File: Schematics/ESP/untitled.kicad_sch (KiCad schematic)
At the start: 10 parts, among them J11 Bumper 1, J12 Bumper 2, J14 Conn_02x19_Odd_Even, J15 UltraSconic B, J16 Conn_02x19_Odd_Even, J2 IMU, J7 UltraSonic A, J8 BLE

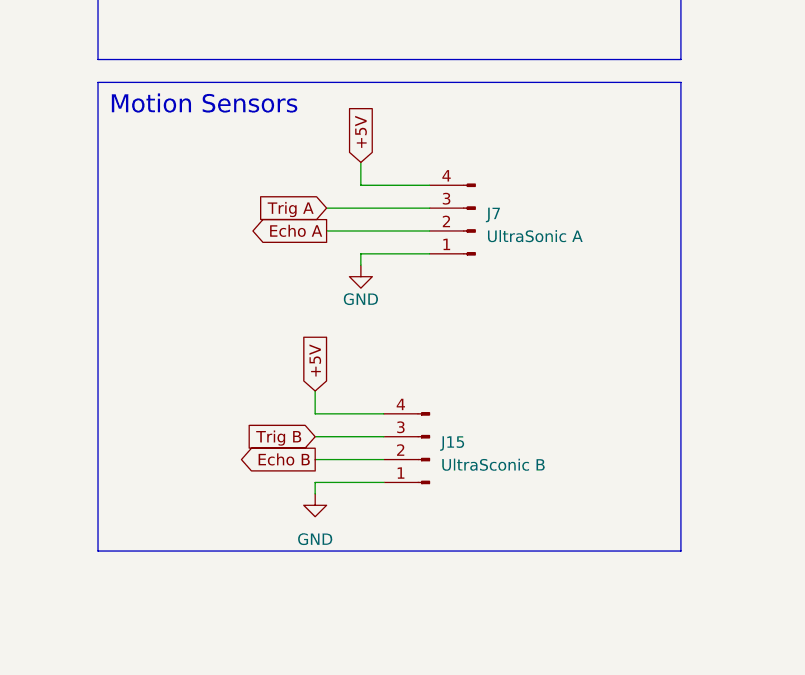
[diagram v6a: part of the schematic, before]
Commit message: PCB layout done no wiring
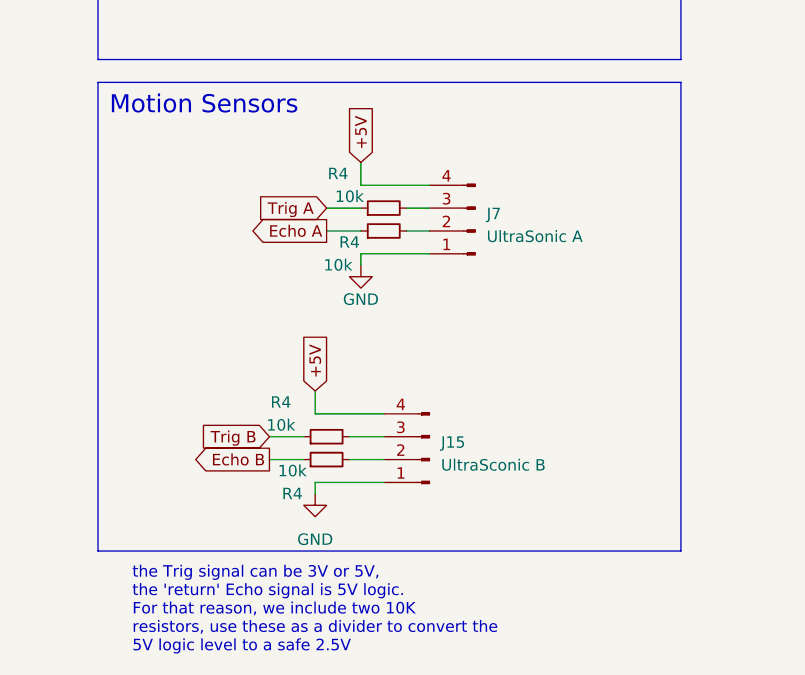
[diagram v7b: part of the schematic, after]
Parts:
- added R4 (x4): 10k, Resistor_SMD:R_1206_3216Metric_Pad1.30x1.75mm_HandSolder, symbol Device:R_Small
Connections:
- net Echo A: now also R4.1; no longer J7.2 (Pin_2)
- net Echo B: now also R4.1; no longer J15.2 (Pin_2)
- net Trig A: now also R4.1; no longer J7.3 (Pin_3)
- net Trig B: now also R4.1; no longer J15.3 (Pin_3)
- new net: J15.3 (Pin_3), R4.2
- new net: J7.3 (Pin_3), R4.2
- new net: J7.2 (Pin_2), R4.2
- new net: J15.2 (Pin_2), R4.2
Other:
- note added: "the Trig signal can be 3V or 5V, the 'return' Echo signal is 5V logic. For that reason, we include two 10K resistors, use these as a divider to convert the 5V logic level to a safe 2.5V"
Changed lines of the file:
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@@
     (stroke (width 0) (type default))
   )
-  (wire (pts (xy 50.8 116.84) (xy 62.23 116.84))
+  (wire (pts (xy 50.8 116.84) (xy 54.61 116.84))
     (stroke (width 0) (type default))
   )
@@
     (stroke (width 0) (type default))
   )
-  (wire (pts (xy 50.8 114.3) (xy 62.23 114.3))
+  (wire (pts (xy 50.8 114.3) (xy 54.61 114.3))
     (stroke (width 0) (type default))
   )
@@
     (stroke (width 0) (type default))
   )
-  (wire (pts (xy 49.53 142.24) (xy 57.15 142.24))
+  (wire (pts (xy 44.45 142.24) (xy 48.26 142.24))
     (stroke (width 0) (type default))
   )
@@
     (stroke (width 0) (type default))
   )
-  (wire (pts (xy 49.53 139.7) (xy 57.15 139.7))
+  (wire (pts (xy 44.45 139.7) (xy 48.26 139.7))
+    (stroke (width 0) (type default))
+  )
+  (wire (pts (xy 53.34 142.24) (xy 57.15 142.24))
     (stroke (width 0) (type default))
   )
@@
     (stroke (width 0) (type default))
   )
+  (wire (pts (xy 53.34 139.7) (xy 57.15 139.7))
+    (stroke (width 0) (type default))
+  )
   (wire (pts (xy 165.1 87.63) (xy 162.56 87.63))
     (stroke (width 0) (type default))
   )
   (wire (pts (xy 246.38 105.41) (xy 242.57 105.41))
+    (stroke (width 0) (type default))
+  )
+  (wire (pts (xy 59.69 114.3) (xy 62.23 114.3))
+    (stroke (width 0) (type default))
+  )
+  (wire (pts (xy 59.69 116.84) (xy 62.23 116.84))
     (stroke (width 0) (type default))
   )
@@
   (text "BLE_RX" (at 254 110.49 0)
     (effects (font (size 1.27 1.27)) (justify right bottom))
+  )
+  (text "the Trig signal can be 3V or 5V,\nthe 'return' Echo signal is 5V logic.\nFor that reason, we include two 10K \nresistors, use these as a divider to convert the \n5V logic level to a safe 2.5V"
+    (at 29.21 163.83 0)
+    (effects (font (size 1.27 1.27)) (justify left bottom))
   )
   (global_label "Bumper Button 2" (shape input) (at 147.32 102.87 180) (fields_autoplaced)
@@
     )
   )
-  (global_label "Trig B" (shape input) (at 49.53 139.7 180) (fields_autoplaced)
+  (global_label "Trig B" (shape input) (at 44.45 139.7 180) (fields_autoplaced)
     (effects (font (size 1.27 1.27)) (justify right))
-    (property "Intersheetrefs" "${INTERSHEET_REFS}" (at 41.0846 139.7 0)
-      (effects (font (size 1.27 1.27)) (justify right) hide)
-    )
-  )
-  (global_label "Echo B" (shape output) (at 49.53 142.24 180) (fields_autoplaced)
+    (property "Intersheetrefs" "${INTERSHEET_REFS}" (at 36.0046 139.7 0)
+      (effects (font (size 1.27 1.27)) (justify right) hide)
+    )
+  )
+  (global_label "Echo B" (shape output) (at 44.45 142.24 180) (fields_autoplaced)
     (effects (font (size 1.27 1.27)) (justify right))
-    (property "Intersheetrefs" "${INTERSHEET_REFS}" (at 40.0566 142.24 0)
+    (property "Intersheetrefs" "${INTERSHEET_REFS}" (at 34.9766 142.24 0)
       (effects (font (size 1.27 1.27)) (justify right) hide)
     )
@@
     )
   )
+  (symbol (lib_id "Device:R_Small") (at 50.8 139.7 90) (unit 1)
+    (in_bom yes) (on_board yes) (dnp no)
+    (property "Reference" "R4" (at 45.72 135.89 90)
+      (effects (font (size 1.27 1.27)))
+    )
+    (property "Value" "10k" (at 45.72 138.43 90)
+      (effects (font (size 1.27 1.27)))
+    )
+    (property "Footprint" "Resistor_SMD:R_1206_3216Metric_Pad1.30x1.75mm_HandSolder" (at 50.8 139.7 0)
+      (effects (font (size 1.27 1.27)) hide)
+    )
+    (property "Datasheet" "https://www.yageo.com/upload/media/product/productsearch/datasheet/rchip/PYu-RC_Group_51_RoHS_L_12.pdf" (at 50.8 139.7 0)
+      (effects (font (size 1.27 1.27)) hide)
+    )
+    (property "digikey link" "https://www.digikey.fi/en/products/detail/yageo/RC1206FR-071KL/728387" (at 50.8 139.7 0)
+      (effects (font (size 1.27 1.27)) hide)
+    )
+    (property "Price" "0,11" (at 50.8 139.7 0)
+      (effects (font (size 1.27 1.27)) hide)
+    )
+    (pin "1")
+    (pin "2")
+    (instances
+      (project "ESP"
+        (path "/b616d203-cf5c-462f-b907-860a8573592a"
+          (reference "R4") (unit 1)
+        )
+        (path "/b616d203-cf5c-462f-b907-860a8573592a/9ad1e8da-d13f-4a6e-8aa2-8655a1d493de"
+          (reference "R12") (unit 1)
+        )
+        (path "/b616d203-cf5c-462f-b907-860a8573592a/d73e0648-2dfb-47f8-9e43-38f378a4f4ca"
+          (reference "R22") (unit 1)
+        )
+      )
+    )
+  )
   (symbol (lib_id "power:GND") (at 242.57 115.57 90) (unit 1)
     (in_bom yes) (on_board yes) (dnp no) (fields_autoplaced)
@@
         (path "/b616d203-cf5c-462f-b907-860a8573592a/d73e0648-2dfb-47f8-9e43-38f378a4f4ca"
           (reference "#PWR026") (unit 1)
+        )
+      )
+    )
+  )
+  (symbol (lib_id "Device:R_Small") (at 57.15 114.3 90) (unit 1)
+    (in_bom yes) (on_board yes) (dnp no)
+    (property "Reference" "R4" (at 52.07 110.49 90)
+      (effects (font (size 1.27 1.27)))
+    )
+    (property "Value" "10k" (at 53.34 113.03 90)
+      (effects (font (size 1.27 1.27)))
+    )
+    (property "Footprint" "Resistor_SMD:R_1206_3216Metric_Pad1.30x1.75mm_HandSolder" (at 57.15 114.3 0)
+      (effects (font (size 1.27 1.27)) hide)
+    )
+    (property "Datasheet" "https://www.yageo.com/upload/media/product/productsearch/datasheet/rchip/PYu-RC_Group_51_RoHS_L_12.pdf" (at 57.15 114.3 0)
+      (effects (font (size 1.27 1.27)) hide)
+    )
+    (property "digikey link" "https://www.digikey.fi/en/products/detail/yageo/RC1206FR-071KL/728387" (at 57.15 114.3 0)
+      (effects (font (size 1.27 1.27)) hide)
+    )
+    (property "Price" "0,11" (at 57.15 114.3 0)
+      (effects (font (size 1.27 1.27)) hide)
+    )
+    (pin "1")
+    (pin "2")
+    (instances
+      (project "ESP"
+        (path "/b616d203-cf5c-462f-b907-860a8573592a"
+          (reference "R4") (unit 1)
+        )
+        (path "/b616d203-cf5c-462f-b907-860a8573592a/9ad1e8da-d13f-4a6e-8aa2-8655a1d493de"
+          (reference "R12") (unit 1)
+        )
+        (path "/b616d203-cf5c-462f-b907-860a8573592a/d73e0648-2dfb-47f8-9e43-38f378a4f4ca"
+          (reference "R15") (unit 1)
         )
       )
@@
     )
   )
+  (symbol (lib_id "Device:R_Small") (at 57.15 116.84 90) (unit 1)
+    (in_bom yes) (on_board yes) (dnp no)
+    (property "Reference" "R4" (at 53.34 118.11 90)
+      (effects (font (size 1.27 1.27)))
+    )
+    (property "Value" "10k" (at 52.07 120.65 90)
+      (effects (font (size 1.27 1.27)))
+    )
+    (property "Footprint" "Resistor_SMD:R_1206_3216Metric_Pad1.30x1.75mm_HandSolder" (at 57.15 116.84 0)
+      (effects (font (size 1.27 1.27)) hide)
+    )
+    (property "Datasheet" "https://www.yageo.com/upload/media/product/productsearch/datasheet/rchip/PYu-RC_Group_51_RoHS_L_12.pdf" (at 57.15 116.84 0)
+      (effects (font (size 1.27 1.27)) hide)
+    )
+    (property "digikey link" "https://www.digikey.fi/en/products/detail/yageo/RC1206FR-071KL/728387" (at 57.15 116.84 0)
+      (effects (font (size 1.27 1.27)) hide)
+    )
+    (property "Price" "0,11" (at 57.15 116.84 0)
+      (effects (font (size 1.27 1.27)) hide)
+    )
+    (pin "1")
+    (pin "2")
+    (instances
+      (project "ESP"
+        (path "/b616d203-cf5c-462f-b907-860a8573592a"
+          (reference "R4") (unit 1)
+        )
+        (path "/b616d203-cf5c-462f-b907-860a8573592a/9ad1e8da-d13f-4a6e-8aa2-8655a1d493de"
+          (reference "R12") (unit 1)
+        )
+        (path "/b616d203-cf5c-462f-b907-860a8573592a/d73e0648-2dfb-47f8-9e43-38f378a4f4ca"
+          (reference "R18") (unit 1)
+        )
+      )
+    )
+  )
   (symbol (lib_id "power:GND") (at 229.87 102.87 270) (unit 1)
     (in_bom yes) (on_board yes) (dnp no) (fields_autoplaced)
@@
         )
       )
+    )
+  )
+  (symbol (lib_id "Device:R_Small") (at 50.8 142.24 90) (unit 1)
+    (in_bom yes) (on_board yes) (dnp no)
+    (property "Reference" "R4" (at 46.99 146.05 90)
+      (effects (font (size 1.27 1.27)))
+    )
+    (property "Value" "10k" (at 46.99 143.51 90)
+      (effects (font (size 1.27 1.27)))
+    )
+    (property "Footprint" "Resistor_SMD:R_1206_3216Metric_Pad1.30x1.75mm_HandSolder" (at 50.8 142.24 0)
+      (effects (font (size 1.27 1.27)) hide)
+    )
+    (property "Datasheet" "https://www.yageo.com/upload/media/product/productsearch/datasheet/rchip/PYu-RC_Group_51_RoHS_L_12.pdf" (at 50.8 142.24 0)
+      (effects (font (size 1.27 1.27)) hide)
+    )
+    (property "digikey link" "https://www.digikey.fi/en/products/detail/yageo/RC1206FR-071KL/728387" (at 50.8 142.24 0)
+      (effects (font (size 1.27 1.27)) hide)
+    )
+    (property "Price" "0,11" (at 50.8 142.24 0)
+      (effects (font (size 1.27 1.27)) hide)
+    )
+    (pin "1")
+    (pin "2")
+    (instances
+      (project "ESP"
+        (path "/b616d203-cf5c-462f-b907-860a8573592a"
+          (reference "R4") (unit 1)
+        )
+        (path "/b616d203-cf5c-462f-b907-860a8573592a/9ad1e8da-d13f-4a6e-8aa2-8655a1d493de"
+          (reference "R12") (unit 1)
+        )
+        (path "/b616d203-cf5c-462f-b907-860a8573592a/d73e0648-2dfb-47f8-9e43-38f378a4f4ca"
+          (reference "R23") (unit 1)
+        )
+      )

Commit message: added esp32 connected
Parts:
- removed J8: BLE, Connector_PinSocket_2.54mm:PinSocket_1x06_P2.54mm_Vertical, symbol Connector:Conn_01x06_Pin
- added J9: ESP, Connector_PinSocket_2.54mm:PinSocket_2x04_P2.54mm_Vertical, symbol Connector_Generic:Conn_02x04_Odd_Even
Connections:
- net GND: now also J9.8 (Pin_8)
- net +3.3V: now reaches J14.16 (Pin_16)
- net +3.3V: now also J9.1 (Pin_1), J9.3 (Pin_3)
- net TX: now reaches J16.21 (Pin_21)
- net TX: now also J9.7 (Pin_7)
- net RX: now reaches J16.31 (Pin_31)
- net RX: now also J9.2 (Pin_2)
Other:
- note removed: "BLE_RX"
- note removed: "BLE_TX"
